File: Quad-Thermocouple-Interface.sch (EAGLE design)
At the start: 17 parts

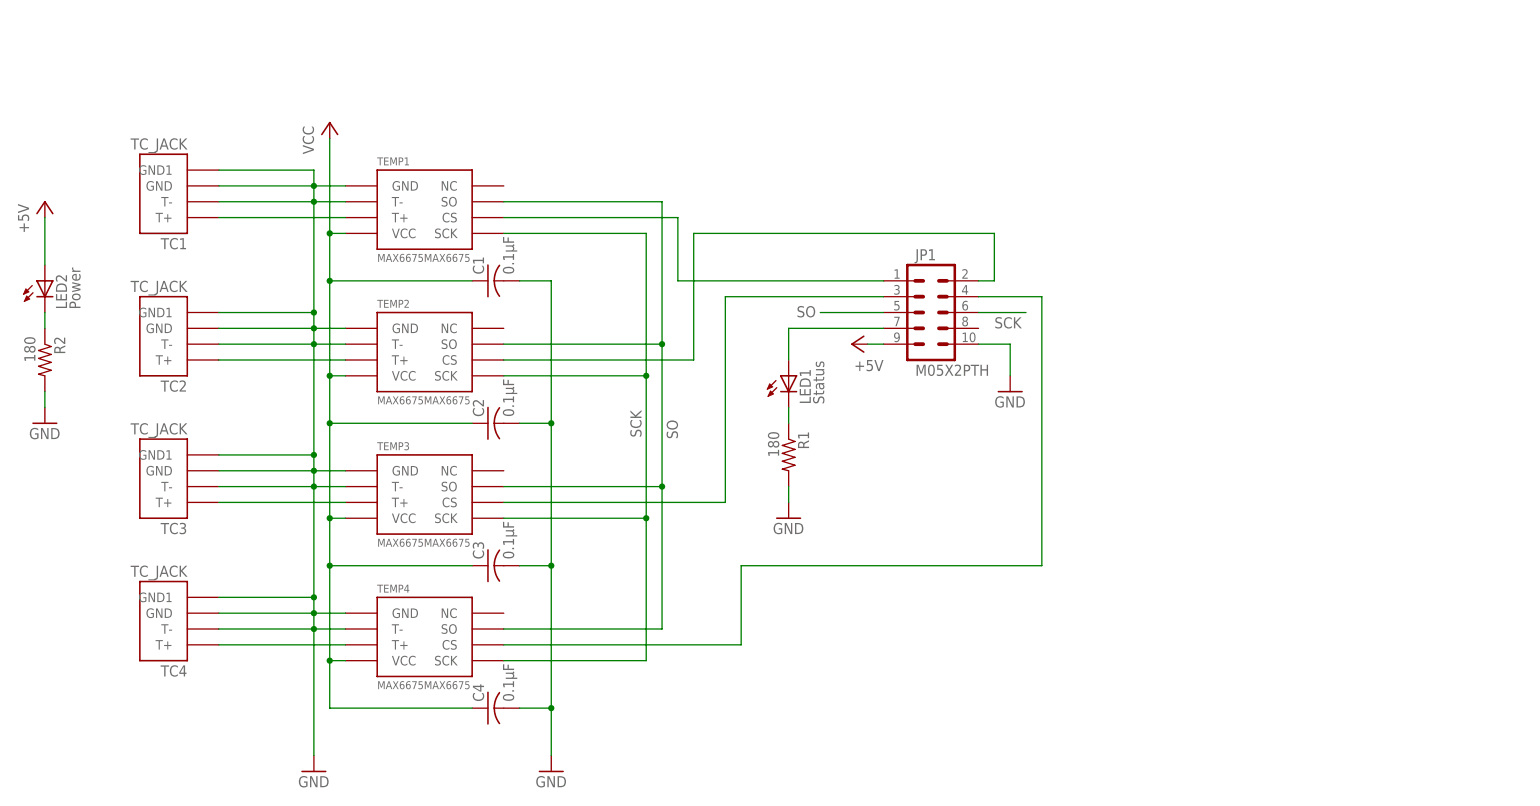
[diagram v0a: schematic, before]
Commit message: Updated with level shifter and power supply for MAX31855, rev to v2.0
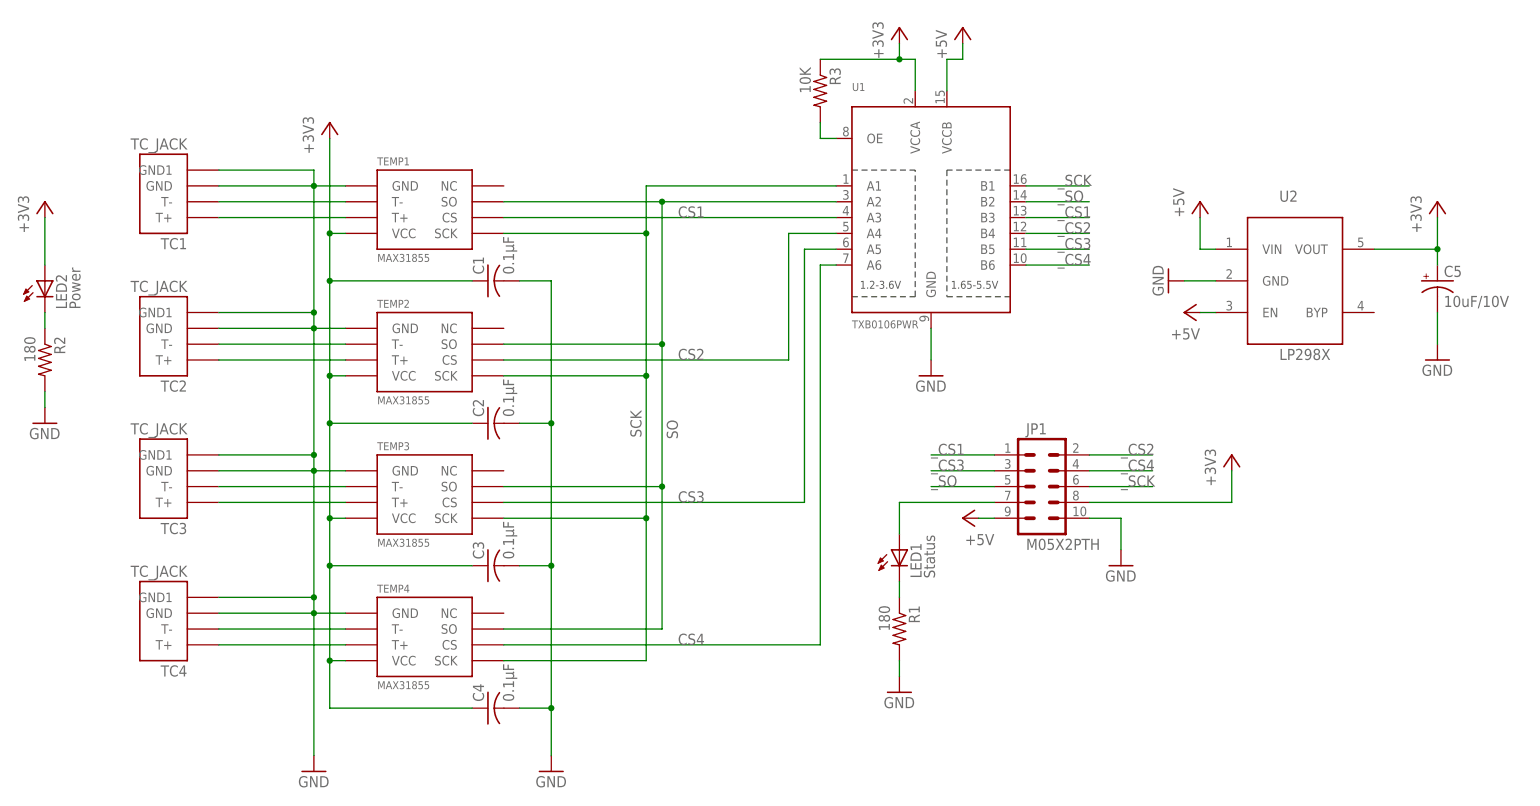
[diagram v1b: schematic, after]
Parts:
- added C5: 10uF/10V, adafruit:CPOL-USA/3216-18R
- added R3: 10K, resistor:R-US_R0603
- added U1: TXB0106PWR, McLEng:TXB0106PWR
- added U2: LP298XS, adafruit:LP298XS
- TEMP1, TEMP2, TEMP3, TEMP4: value MAX6675MAX6675 -> MAX31855; device McLEng:MAX6675MAX6675 -> McLEng:MAX6675MAX31855
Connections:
- net N$1 renamed LED1
- net N$12 renamed T4
- net N$3 renamed T1
- net N$6 renamed T2
- net N$9 renamed T3
- removed net VCC: C1.1, C2.1, C3.1, C4.1, JP1.9, LED2.A, TEMP1.VCC, TEMP2.VCC, TEMP3.VCC, TEMP4.VCC
- new net +3V3: C1.1, C2.1, C3.1, C4.1, C5.+, JP1.8, LED2.A, R3.1, TEMP1.VCC, TEMP2.VCC, TEMP3.VCC, TEMP4.VCC, U1.VCCA, U2.VOUT
- new net +5V: JP1.9, U1.VCCB, U2.EN, U2.VIN
- new net N$1: R3.2, U1.OE
- new net T1-: TC1.T-, TEMP1.T-
- new net T2-: TC2.T-, TEMP2.T-
- new net T3-: TC3.T-, TEMP3.T-
- new net T4-: TC4.T-, TEMP4.T-
- new net _CS1: JP1.1, U1.B3
- new net _CS2: JP1.2, U1.B4
- new net _CS3: JP1.3, U1.B5
- new net _CS4: JP1.4, U1.B6
- new net _SCK: JP1.6, U1.B1
- new net _SO: JP1.5, U1.B2
- net CS1: now also U1.A3; no longer JP1.1
- net CS2: now also U1.A4; no longer JP1.2
- net CS3: now also U1.A5; no longer JP1.3
- net CS4: now also U1.A6; no longer JP1.4
- net GND: now also C5.-, U1.GND, U2.GND; no longer TC1.T-, TC2.T-, TC3.T-, TC4.T-, TEMP1.T-, TEMP2.T-, TEMP3.T-, TEMP4.T-
- net SCK: now also U1.A1; no longer JP1.6
- net SO: now also U1.A2; no longer JP1.5
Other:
- moved on the sheet: JP1, LED1, R1
